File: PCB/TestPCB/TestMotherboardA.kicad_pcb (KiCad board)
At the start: 2 copper layers, 61.2 x 100.1 mm, 30 parts, among them M2 Screw MountingHole_2.2mm_M2

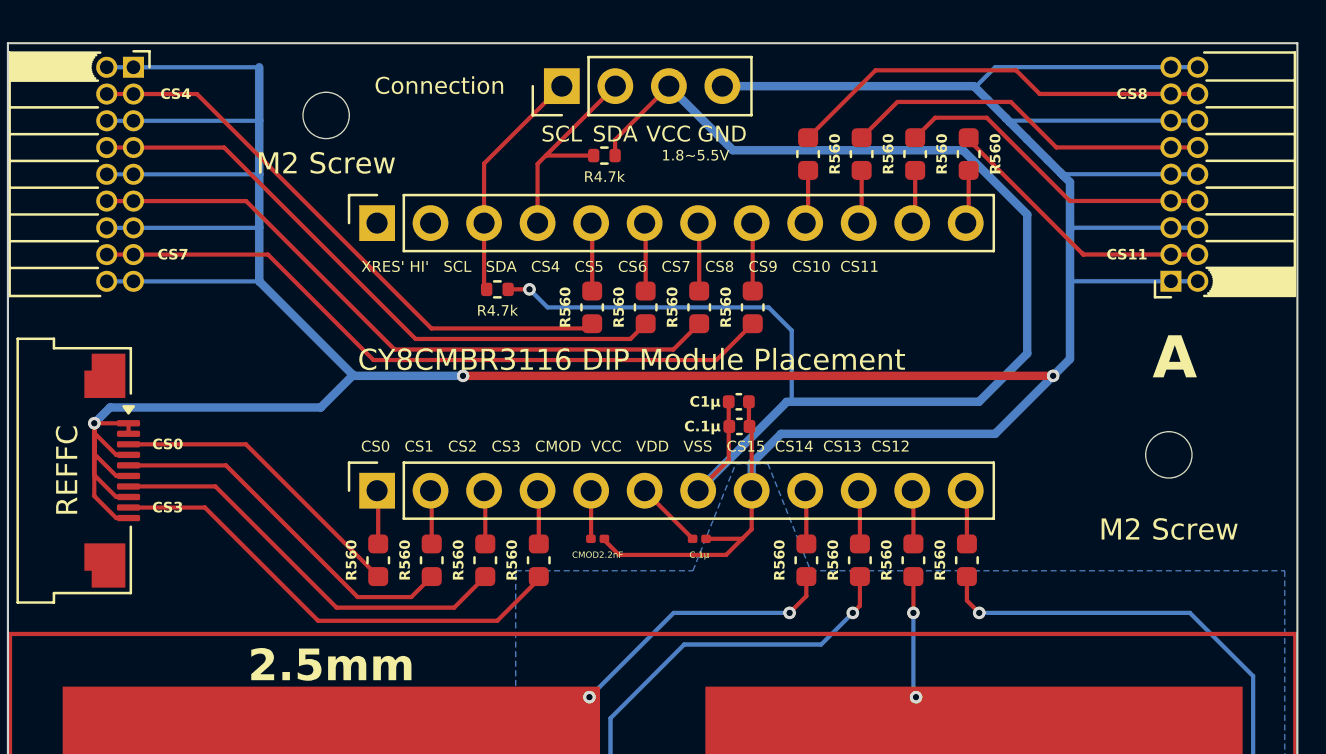
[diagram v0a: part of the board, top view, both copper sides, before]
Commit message: Modify test pcb, add flow chart
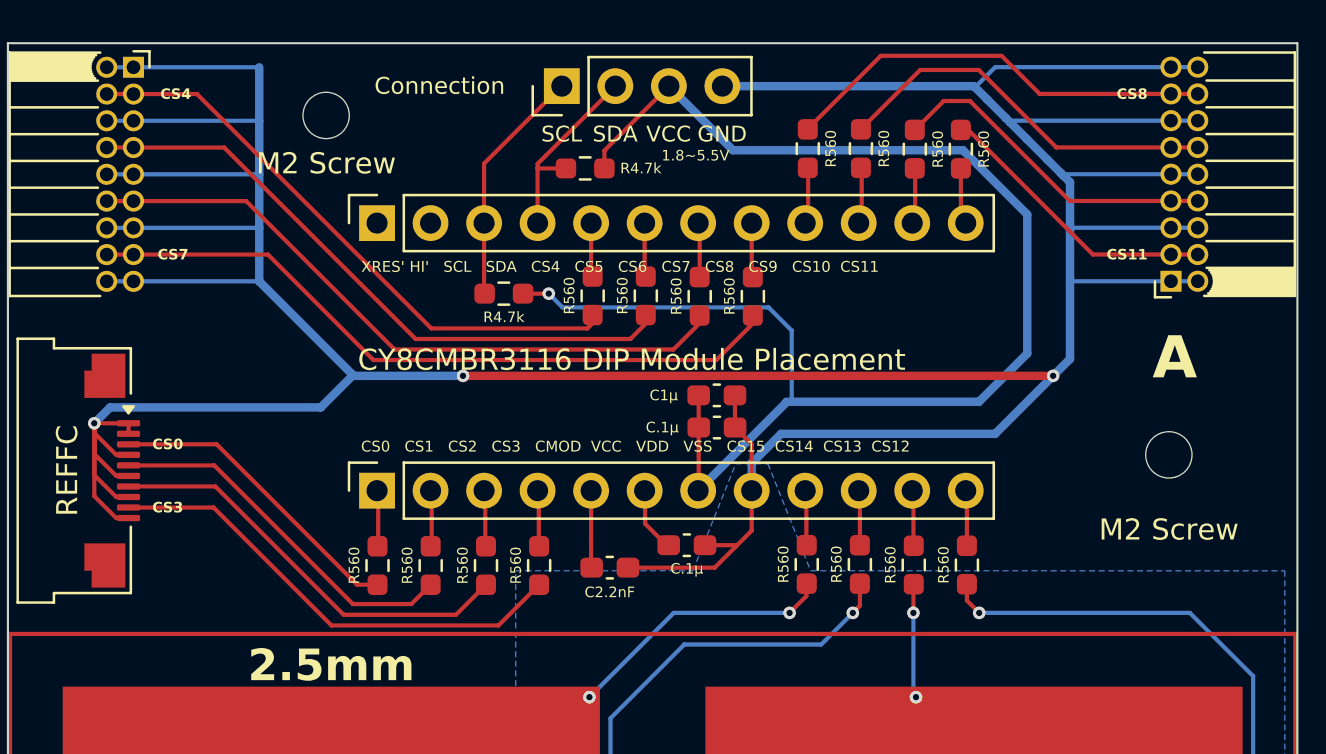
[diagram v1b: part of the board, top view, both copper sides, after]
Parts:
- removed the R560 at (54.8, 38.0)
- removed the R560 at (44.6, 26.0)
- removed the R560 at (42.1, 38.0)
- removed the R560 at (37.0, 38.0)
- removed the R560 at (52.2, 26.0)
- removed the R560 at (59.9, 38.0)
- removed the R560 at (49.7, 26.0)
- removed the R560 at (47.2, 26.0)
- removed the R560 at (54.9, 18.7)
- removed the R560 at (57.3, 38.0)
- removed the R560 at (39.6, 38.0)
- removed the R560 at (60.0, 18.7)
- removed the R560 at (34.5, 38.0)
- removed the R560 at (62.5, 18.7)
- removed the R560 at (57.4, 18.7)
- added R560: R_0603_1608Metric_Pad0.98x0.95mm_HandSolder, Resistor_SMD:R_0603_1608Metric_Pad0.98x0.95mm_HandSolder, F.Cu at (54.9, 18.5)
- added R560: R_0603_1608Metric_Pad0.98x0.95mm_HandSolder, Resistor_SMD:R_0603_1608Metric_Pad0.98x0.95mm_HandSolder, F.Cu at (39.6, 38.3)
- added R560: R_0603_1608Metric_Pad0.98x0.95mm_HandSolder, Resistor_SMD:R_0603_1608Metric_Pad0.98x0.95mm_HandSolder, F.Cu at (49.7, 25.5)
- added R560: R_0603_1608Metric_Pad0.98x0.95mm_HandSolder, Resistor_SMD:R_0603_1608Metric_Pad0.98x0.95mm_HandSolder, F.Cu at (52.3, 25.5)
- added R560: R_0603_1608Metric_Pad0.98x0.95mm_HandSolder, Resistor_SMD:R_0603_1608Metric_Pad0.98x0.95mm_HandSolder, F.Cu at (34.4, 38.3)
- added R560: R_0603_1608Metric_Pad0.98x0.95mm_HandSolder, Resistor_SMD:R_0603_1608Metric_Pad0.98x0.95mm_HandSolder, F.Cu at (42.1, 38.3)
- added R560: R_0603_1608Metric_Pad0.98x0.95mm_HandSolder, Resistor_SMD:R_0603_1608Metric_Pad0.98x0.95mm_HandSolder, F.Cu at (54.8, 38.2)
- added R560: R_0603_1608Metric_Pad0.98x0.95mm_HandSolder, Resistor_SMD:R_0603_1608Metric_Pad0.98x0.95mm_HandSolder, F.Cu at (62.1, 18.5)
- added R560: R_0603_1608Metric_Pad0.98x0.95mm_HandSolder, Resistor_SMD:R_0603_1608Metric_Pad0.98x0.95mm_HandSolder, F.Cu at (57.3, 38.2)
- added R560: R_0603_1608Metric_Pad0.98x0.95mm_HandSolder, Resistor_SMD:R_0603_1608Metric_Pad0.98x0.95mm_HandSolder, F.Cu at (47.2, 25.5)
- added R560: R_0603_1608Metric_Pad0.98x0.95mm_HandSolder, Resistor_SMD:R_0603_1608Metric_Pad0.98x0.95mm_HandSolder, F.Cu at (44.7, 25.5)
- added R560: R_0603_1608Metric_Pad0.98x0.95mm_HandSolder, Resistor_SMD:R_0603_1608Metric_Pad0.98x0.95mm_HandSolder, F.Cu at (57.4, 18.5)
- added R560: R_0603_1608Metric_Pad0.98x0.95mm_HandSolder, Resistor_SMD:R_0603_1608Metric_Pad0.98x0.95mm_HandSolder, F.Cu at (59.9, 38.2)
- added R560: R_0603_1608Metric_Pad0.98x0.95mm_HandSolder, Resistor_SMD:R_0603_1608Metric_Pad0.98x0.95mm_HandSolder, F.Cu at (59.9, 18.5)
- added R560: R_0603_1608Metric_Pad0.98x0.95mm_HandSolder, Resistor_SMD:R_0603_1608Metric_Pad0.98x0.95mm_HandSolder, F.Cu at (37.0, 38.3)
- C.1μ: value C_0201_0603Metric -> C_0603_1608Metric_Pad1.08x0.95mm_HandSolder; footprint Capacitor_SMD:C_0201_0603Metric -> Capacitor_SMD:C_0603_1608Metric_Pad1.08x0.95mm_HandSolder
- C.1μ, C1μ: value C_0402_1005Metric -> C_0603_1608Metric_Pad1.08x0.95mm_HandSolder; footprint Capacitor_SMD:C_0402_1005Metric -> Capacitor_SMD:C_0603_1608Metric_Pad1.08x0.95mm_HandSolder
- C2.2nF: renamed from CMOD2.2nF; value C_0201_0603Metric -> C_0603_1608Metric_Pad1.08x0.95mm_HandSolder; footprint Capacitor_SMD:C_0201_0603Metric -> Capacitor_SMD:C_0603_1608Metric_Pad1.08x0.95mm_HandSolder
- R4.7k (x2): value R_0402_1005Metric -> R_0603_1608Metric_Pad0.98x0.95mm_HandSolder; footprint Resistor_SMD:R_0402_1005Metric -> Resistor_SMD:R_0603_1608Metric_Pad0.98x0.95mm_HandSolder
- R560: value C_0603_1608Metric -> R_0603_1608Metric_Pad0.98x0.95mm_HandSolder; footprint Capacitor_SMD:C_0603_1608Metric -> Resistor_SMD:R_0603_1608Metric_Pad0.98x0.95mm_HandSolder
- moved C2.2nF 1.48 mm to (45.5, 38.4)
- moved R4.7k 1.10 mm to (44.3, 19.4)
- moved C1μ 1.09 mm to (50.5, 30.2)
- moved C.1μ 1.07 mm to (50.6, 31.7)
- moved C.1μ 0.66 mm to (49.1, 37.3)
- moved R4.7k 0.37 mm to (40.4, 25.3)
- moved R560 0.22 mm to (62.4, 38.2)
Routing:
- net TP: track 384.7 -> 387.4 mm
- net R-CS: track 42.1 -> 39.9 mm
- net CMOD: track 2.29 -> 3.68 mm
- net I²C: track 21.5 -> 20.8 mm
- net GND: track 216.8 -> 216.2 mm
